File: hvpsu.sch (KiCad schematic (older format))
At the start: 18 parts, among them P1 CONN_01X02, P2 CONN_01X02, SW1 Switch_DPST

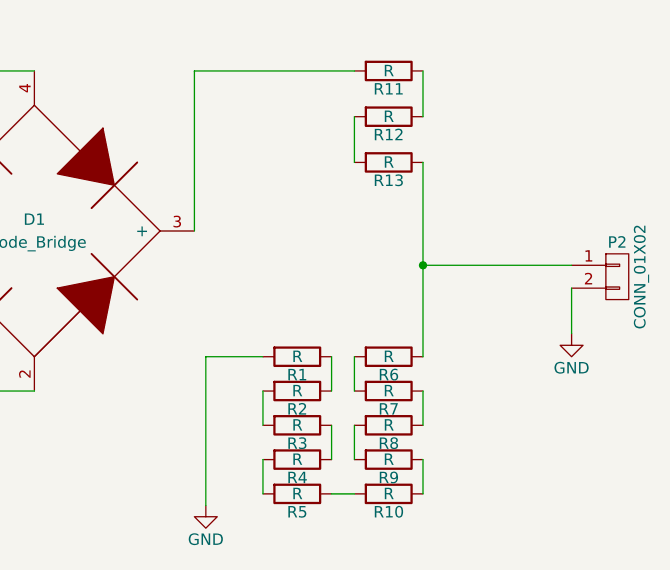
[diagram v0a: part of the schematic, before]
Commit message: fitlering cap and annotations
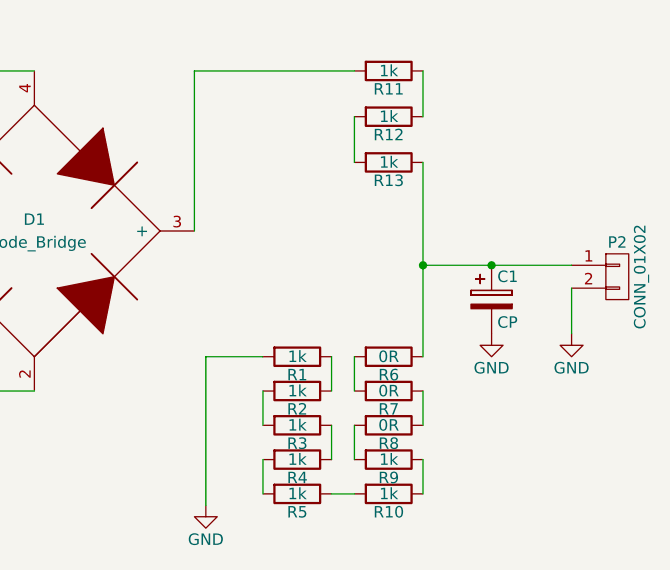
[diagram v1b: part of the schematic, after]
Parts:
- added C1: CP, symbol CP
- R1, R10, R11, R12, R13, R2, R3, R4, R5, R9: value R -> 1k
- R6, R7, R8: value R -> 0R
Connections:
- net GND: now also C1.2
- net at P2.1 (P1), R13.1, R6.1: now also C1.1
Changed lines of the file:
@@
 P 5650 1300
 F 0 "R11" V 5730 1300 50  0000 C CNN
-F 1 "R" V 5650 1300 50  0000 C CNN
+F 1 "1k" V 5650 1300 50  0000 C CNN
 F 2 "" V 5580 1300 30  0000 C CNN
 F 3 "" H 5650 1300 30  0000 C CNN
@@
 P 5650 1500
 F 0 "R12" V 5730 1500 50  0000 C CNN
-F 1 "R" V 5650 1500 50  0000 C CNN
+F 1 "1k" V 5650 1500 50  0000 C CNN
 F 2 "" V 5580 1500 30  0000 C CNN
 F 3 "" H 5650 1500 30  0000 C CNN
@@
 P 5650 1700
 F 0 "R13" V 5730 1700 50  0000 C CNN
-F 1 "R" V 5650 1700 50  0000 C CNN
+F 1 "1k" V 5650 1700 50  0000 C CNN
 F 2 "" V 5580 1700 30  0000 C CNN
 F 3 "" H 5650 1700 30  0000 C CNN
@@
 P 5250 3150
 F 0 "R5" V 5330 3150 50  0000 C CNN
-F 1 "R" V 5250 3150 50  0000 C CNN
+F 1 "1k" V 5250 3150 50  0000 C CNN
 F 2 "" V 5180 3150 30  0000 C CNN
 F 3 "" H 5250 3150 30  0000 C CNN
@@
 P 5250 3000
 F 0 "R4" V 5330 3000 50  0000 C CNN
-F 1 "R" V 5250 3000 50  0000 C CNN
+F 1 "1k" V 5250 3000 50  0000 C CNN
 F 2 "" V 5180 3000 30  0000 C CNN
 F 3 "" H 5250 3000 30  0000 C CNN
@@
 P 5250 2850
 F 0 "R3" V 5330 2850 50  0000 C CNN
-F 1 "R" V 5250 2850 50  0000 C CNN
+F 1 "1k" V 5250 2850 50  0000 C CNN
 F 2 "" V 5180 2850 30  0000 C CNN
 F 3 "" H 5250 2850 30  0000 C CNN
@@
 P 5250 2700
 F 0 "R2" V 5330 2700 50  0000 C CNN
-F 1 "R" V 5250 2700 50  0000 C CNN
+F 1 "1k" V 5250 2700 50  0000 C CNN
 F 2 "" V 5180 2700 30  0000 C CNN
 F 3 "" H 5250 2700 30  0000 C CNN
@@
 P 5250 2550
 F 0 "R1" V 5330 2550 50  0000 C CNN
-F 1 "R" V 5250 2550 50  0000 C CNN
+F 1 "1k" V 5250 2550 50  0000 C CNN
 F 2 "" V 5180 2550 30  0000 C CNN
 F 3 "" H 5250 2550 30  0000 C CNN
 	1    5250 2550
-	0    1    1    0
-$EndComp
-$Comp
-L R R6
-U 1 1 557434CE
-P 5650 2550
-F 0 "R6" V 5730 2550 50  0000 C CNN
-F 1 "R" V 5650 2550 50  0000 C CNN
-F 2 "" V 5580 2550 30  0000 C CNN
-F 3 "" H 5650 2550 30  0000 C CNN
-	1    5650 2550
-	0    1    1    0
-$EndComp
-$Comp
-L R R7
-U 1 1 5574350A
-P 5650 2700
-F 0 "R7" V 5730 2700 50  0000 C CNN
-F 1 "R" V 5650 2700 50  0000 C CNN
-F 2 "" V 5580 2700 30  0000 C CNN
-F 3 "" H 5650 2700 30  0000 C CNN
-	1    5650 2700
-	0    1    1    0
-$EndComp
-$Comp
-L R R8
-U 1 1 5574353C
-P 5650 2850
-F 0 "R8" V 5730 2850 50  0000 C CNN
-F 1 "R" V 5650 2850 50  0000 C CNN
-F 2 "" V 5580 2850 30  0000 C CNN
-F 3 "" H 5650 2850 30  0000 C CNN
-	1    5650 2850
 	0    1    1    0
 $EndComp
@@
 P 5650 3000
 F 0 "R9" V 5730 3000 50  0000 C CNN
-F 1 "R" V 5650 3000 50  0000 C CNN
+F 1 "1k" V 5650 3000 50  0000 C CNN
 F 2 "" V 5580 3000 30  0000 C CNN
 F 3 "" H 5650 3000 30  0000 C CNN
@@
 P 5650 3150
 F 0 "R10" V 5730 3150 50  0000 C CNN
-F 1 "R" V 5650 3150 50  0000 C CNN
+F 1 "1k" V 5650 3150 50  0000 C CNN
 F 2 "" V 5580 3150 30  0000 C CNN
 F 3 "" H 5650 3150 30  0000 C CNN
@@
 	0    1    1    0
 $EndComp
-Wire Wire Line
-	900  1300 1800 1300
-Wire Wire Line
-	900  1700 1800 1700
-Wire Wire Line
-	2400 1300 2950 1300
-Wire Wire Line
-	3450 1300 4100 1300
-Wire Wire Line
-	3400 2000 3400 3200
-Wire Wire Line
-	4100 2700 3150 2700
-Wire Wire Line
-	3150 2700 3150 1700
-Wire Wire Line
-	3150 1700 2400 1700
-Wire Wire Line
-	4800 2000 4800 1300
-Wire Wire Line
-	4800 1300 5500 1300
-Wire Wire Line
-	5800 1300 5800 1500
-Wire Wire Line
-	5500 1500 5500 1700
-Wire Wire Line
-	5800 1700 5800 2550
-Wire Wire Line
-	5100 2550 4850 2550
-Wire Wire Line
-	4850 2550 4850 3200
-Wire Wire Line
-	5400 2550 5400 2700
-Wire Wire Line
-	5100 2700 5100 2850
-Wire Wire Line
-	5400 2850 5400 3000
-Wire Wire Line
-	5100 3000 5100 3150
-Wire Wire Line
-	5400 3150 5500 3150
-Wire Wire Line
-	5800 3150 5800 3000
-Wire Wire Line
-	5500 3000 5500 2850
-Wire Wire Line
-	5800 2850 5800 2700
-Wire Wire Line
-	5500 2700 5500 2550
-$Comp
-L GND #PWR1
+$Comp
+L GND #PWR01
 U 1 1 557438FF
 P 3400 3200
-F 0 "#PWR1" H 3400 2950 50  0001 C CNN
+F 0 "#PWR01" H 3400 2950 50  0001 C CNN
 F 1 "GND" H 3400 3050 50  0000 C CNN
 F 2 "" H 3400 3200 60  0000 C CNN
@@
 $EndComp
 $Comp
-L GND #PWR2
+L GND #PWR02
 U 1 1 55743931
 P 4850 3200
-F 0 "#PWR2" H 4850 2950 50  0001 C CNN
+F 0 "#PWR02" H 4850 2950 50  0001 C CNN
 F 1 "GND" H 4850 3050 50  0000 C CNN
 F 2 "" H 4850 3200 60  0000 C CNN
@@
 	1    0    0    -1
 $EndComp
-Wire Wire Line
-	5800 2150 6450 2150
-Connection ~ 5800 2150
-$Comp
-L GND #PWR3
+$Comp
+L GND #PWR03
 U 1 1 55743988
 P 6450 2450
-F 0 "#PWR3" H 6450 2200 50  0001 C CNN
+F 0 "#PWR03" H 6450 2200 50  0001 C CNN
 F 1 "GND" H 6450 2300 50  0000 C CNN
 F 2 "" H 6450 2450 60  0000 C CNN
@@
 	1    0    0    -1
 $EndComp
-Wire Wire Line
-	6450 2250 6450 2450
 $Comp
 L CONN_01X02 P1
@@
 	-1   0    0    1
 $EndComp
-Wire Wire Line
-	900  1300 900  1450
-Wire Wire Line
-	900  1700 900  1550
 $Comp
 L CONN_01X02 P2
@@
 $EndComp
 $Comp
-L PWR_FLAG #FLG1
+L PWR_FLAG #FLG04
 U 1 1 55743C8C
 P 1800 1300
-F 0 "#FLG1" H 1800 1395 50  0001 C CNN
+F 0 "#FLG04" H 1800 1395 50  0001 C CNN
 F 1 "PWR_FLAG" H 1800 1480 50  0000 C CNN
 F 2 "" H 1800 1300 60  0000 C CNN
@@
 $EndComp
 $Comp
-L PWR_FLAG #FLG2
+L PWR_FLAG #FLG05
 U 1 1 55743CFC
 P 2400 1300
-F 0 "#FLG2" H 2400 1395 50  0001 C CNN
+F 0 "#FLG05" H 2400 1395 50  0001 C CNN
 F 1 "PWR_FLAG" H 2400 1480 50  0000 C CNN
 F 2 "" H 2400 1300 60  0000 C CNN
@@
 $EndComp
 $Comp
-L PWR_FLAG #FLG5
+L PWR_FLAG #FLG06
 U 1 1 55743E75
 P 3450 1300
-F 0 "#FLG5" H 3450 1395 50  0001 C CNN
+F 0 "#FLG06" H 3450 1395 50  0001 C CNN
 F 1 "PWR_FLAG" H 3450 1480 50  0000 C CNN
 F 2 "" H 3450 1300 60  0000 C CNN
@@
 $EndComp
 $Comp
-L PWR_FLAG #FLG4
+L PWR_FLAG #FLG07
 U 1 1 557443CE
 P 3400 2000
-F 0 "#FLG4" H 3400 2095 50  0001 C CNN
+F 0 "#FLG07" H 3400 2095 50  0001 C CNN
 F 1 "PWR_FLAG" H 3400 2180 50  0000 C CNN
 F 2 "" H 3400 2000 60  0000 C CNN
@@
 $EndComp
 $Comp
-L PWR_FLAG #FLG3
+L PWR_FLAG #FLG08
 U 1 1 55744472
 P 3150 1700
-F 0 "#FLG3" H 3150 1795 50  0001 C CNN
+F 0 "#FLG08" H 3150 1795 50  0001 C CNN
 F 1 "PWR_FLAG" H 3150 1880 50  0000 C CNN
 F 2 "" H 3150 1700 60  0000 C CNN
@@
 	1    0    0    -1
 $EndComp
+$Comp
+L CP C1
+U 1 1 5574485B
+P 6100 2300
+F 0 "C1" H 6125 2400 50  0000 L CNN
+F 1 "CP" H 6125 2200 50  0000 L CNN
+F 2 "" H 6138 2150 30  0000 C CNN
+F 3 "" H 6100 2300 60  0000 C CNN
+	1    6100 2300
+	1    0    0    -1
+$EndComp
+$Comp
+L GND #PWR09
+U 1 1 557448C8
+P 6100 2450
+F 0 "#PWR09" H 6100 2200 50  0001 C CNN
+F 1 "GND" H 6100 2300 50  0000 C CNN
+F 2 "" H 6100 2450 60  0000 C CNN
+F 3 "" H 6100 2450 60  0000 C CNN
+	1    6100 2450
+	1    0    0    -1
+$EndComp
+Wire Wire Line
+	900  1300 1800 1300
+Wire Wire Line
+	900  1700 1800 1700
+Wire Wire Line
+	2400 1300 2950 1300
+Wire Wire Line
+	3450 1300 4100 1300
+Wire Wire Line
+	3400 2000 3400 3200
+Wire Wire Line
+	4100 2700 3150 2700
+Wire Wire Line
+	3150 2700 3150 1700
+Wire Wire Line
+	3150 1700 2400 1700
+Wire Wire Line
+	4800 2000 4800 1300
+Wire Wire Line
+	4800 1300 5500 1300
+Wire Wire Line
+	5800 1300 5800 1500
+Wire Wire Line
+	5500 1500 5500 1700
+Wire Wire Line
+	5800 1700 5800 2550
+Wire Wire Line
+	5100 2550 4850 2550
+Wire Wire Line
+	4850 2550 4850 3200
+Wire Wire Line
+	5400 2550 5400 2700
+Wire Wire Line
+	5100 2700 5100 2850
+Wire Wire Line
+	5400 2850 5400 3000
+Wire Wire Line
+	5100 3000 5100 3150
+Wire Wire Line
+	5400 3150 5500 3150
+Wire Wire Line
+	5800 3150 5800 3000
+Wire Wire Line
+	5500 3000 5500 2850
+Wire Wire Line
+	5800 2150 6450 2150
+Connection ~ 5800 2150
+Wire Wire Line
+	6450 2250 6450 2450
+Wire Wire Line
+	900  1300 900  1450
+Wire Wire Line
+	900  1700 900  1550
+Connection ~ 6100 2150
+Wire Wire Line
+	5500 2700 5500 2550
+Wire Wire Line
+	5800 2850 5800 2700
+$Comp
+L R R8
+U 1 1 5574353C
+P 5650 2850
+F 0 "R8" V 5730 2850 50  0000 C CNN
+F 1 "0R" V 5650 2850 50  0000 C CNN
+F 2 "" V 5580 2850 30  0000 C CNN
+F 3 "" H 5650 2850 30  0000 C CNN
+	1    5650 2850
+	0    1    1    0
+$EndComp
+$Comp
+L R R7
+U 1 1 5574350A
+P 5650 2700
+F 0 "R7" V 5730 2700 50  0000 C CNN
+F 1 "0R" V 5650 2700 50  0000 C CNN
+F 2 "" V 5580 2700 30  0000 C CNN
+F 3 "" H 5650 2700 30  0000 C CNN
+	1    5650 2700
+	0    1    1    0
+$EndComp
+$Comp
+L R R6
+U 1 1 557434CE
+P 5650 2550
+F 0 "R6" V 5730 2550 50  0000 C CNN
+F 1 "0R" V 5650 2550 50  0000 C CNN
+F 2 "" V 5580 2550 30  0000 C CNN
+F 3 "" H 5650 2550 30  0000 C CNN
+	1    5650 2550
+	0    1    1    0
+$EndComp
 $EndSCHEMATC

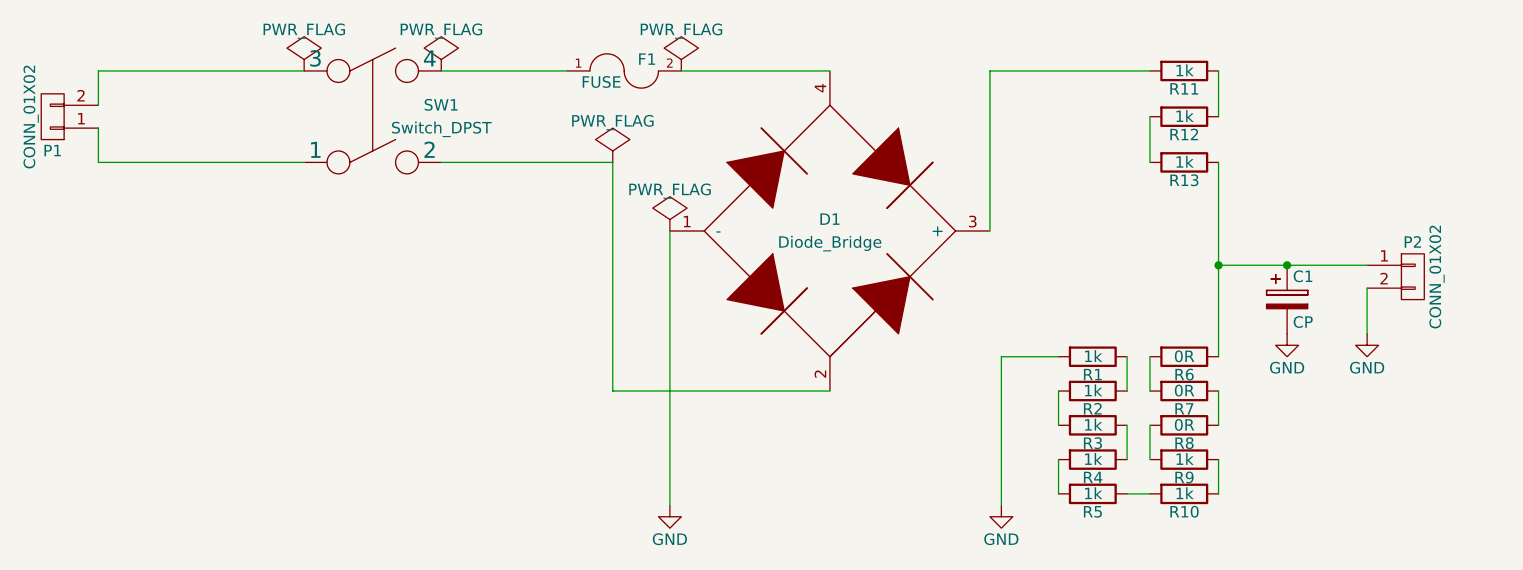
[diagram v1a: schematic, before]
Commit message: most footprints added
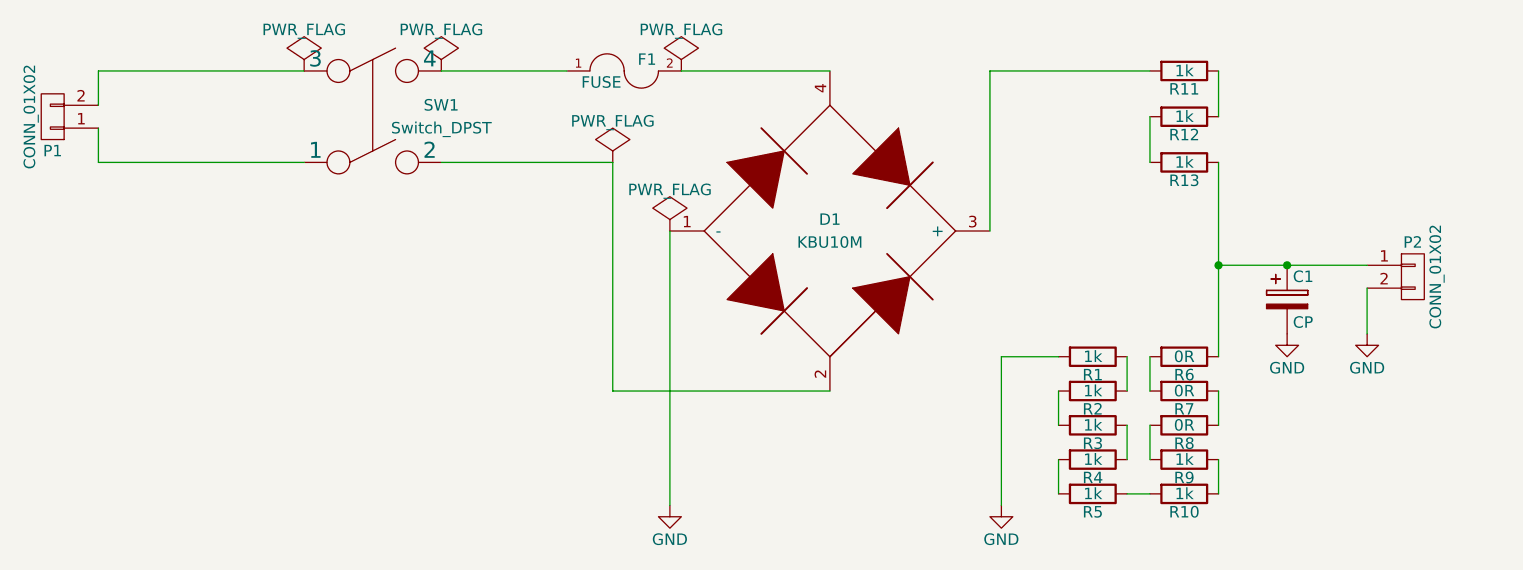
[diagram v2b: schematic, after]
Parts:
- D1: value Diode_Bridge -> KBU10M
- F1: footprint (none) -> Fuse_Holders_and_Fuses:Fuseholder5x20_horiz_open_universal_Type-III
- P1, P2: footprint (none) -> Terminal_Blocks:TerminalBlock_WAGO-236_2Stift_RM5mm_2pol
- R1, R10, R11, R12, R13, R2, R3, R4, R5, R6, R7, R9: footprint (none) -> Resistors_ThroughHole:Resistor_Ceramic_Horizontal_L65mm-W16mm-H15mm-p80mm
- SW1: footprint (none) -> switches:DPST_Rocker_Switch_Chily_3024_Angled
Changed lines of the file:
@@
 LIBS:contrib
 LIBS:valves
+LIBS:hvpsu-cache
 EELAYER 25 0
 EELAYER END
@@
 P 4100 2000
 F 0 "D1" H 4100 2050 50  0000 C CNN
-F 1 "Diode_Bridge" H 4100 1950 50  0000 C CNN
+F 1 "KBU10M" H 4100 1950 50  0000 C CNN
 F 2 "" H 4100 2000 60  0000 C CNN
 F 3 "" H 4100 2000 60  0000 C CNN
@@
 F 0 "F1" H 3300 1350 50  0000 C CNN
 F 1 "FUSE" H 3100 1250 50  0000 C CNN
-F 2 "" H 3200 1300 60  0000 C CNN
+F 2 "Fuse_Holders_and_Fuses:Fuseholder5x20_horiz_open_universal_Type-III" H 3200 1300 60  0001 C CNN
 F 3 "" H 3200 1300 60  0000 C CNN
 	1    3200 1300
@@
 F 0 "SW1" H 2400 1550 50  0000 C CNN
 F 1 "Switch_DPST" H 2400 1450 50  0000 C CNN
-F 2 "" H 2100 1500 60  0000 C CNN
+F 2 "switches:DPST_Rocker_Switch_Chily_3024_Angled" H 2100 1500 60  0001 C CNN
 F 3 "" H 2100 1500 60  0000 C CNN
 	1    2100 1500
@@
 F 0 "R11" V 5730 1300 50  0000 C CNN
 F 1 "1k" V 5650 1300 50  0000 C CNN
-F 2 "" V 5580 1300 30  0000 C CNN
-F 3 "" H 5650 1300 30  0000 C CNN
+F 2 "Resistors_ThroughHole:Resistor_Ceramic_Horizontal_L65mm-W16mm-H15mm-p80mm" V 5580 1300 30  0001 C CNN
+F 3 "" H 5650 1300 30  0001 C CNN
 	1    5650 1300
 	0    1    1    0
@@
 F 0 "R12" V 5730 1500 50  0000 C CNN
 F 1 "1k" V 5650 1500 50  0000 C CNN
-F 2 "" V 5580 1500 30  0000 C CNN
+F 2 "Resistors_ThroughHole:Resistor_Ceramic_Horizontal_L65mm-W16mm-H15mm-p80mm" V 5580 1500 30  0001 C CNN
 F 3 "" H 5650 1500 30  0000 C CNN
 	1    5650 1500
@@
 F 0 "R13" V 5730 1700 50  0000 C CNN
 F 1 "1k" V 5650 1700 50  0000 C CNN
-F 2 "" V 5580 1700 30  0000 C CNN
+F 2 "Resistors_ThroughHole:Resistor_Ceramic_Horizontal_L65mm-W16mm-H15mm-p80mm" V 5580 1700 30  0001 C CNN
 F 3 "" H 5650 1700 30  0000 C CNN
 	1    5650 1700
@@
 F 0 "R5" V 5330 3150 50  0000 C CNN
 F 1 "1k" V 5250 3150 50  0000 C CNN
-F 2 "" V 5180 3150 30  0000 C CNN
+F 2 "Resistors_ThroughHole:Resistor_Ceramic_Horizontal_L65mm-W16mm-H15mm-p80mm" V 5180 3150 30  0001 C CNN
 F 3 "" H 5250 3150 30  0000 C CNN
 	1    5250 3150
@@
 F 0 "R4" V 5330 3000 50  0000 C CNN
 F 1 "1k" V 5250 3000 50  0000 C CNN
-F 2 "" V 5180 3000 30  0000 C CNN
+F 2 "Resistors_ThroughHole:Resistor_Ceramic_Horizontal_L65mm-W16mm-H15mm-p80mm" V 5180 3000 30  0001 C CNN
 F 3 "" H 5250 3000 30  0000 C CNN
 	1    5250 3000
@@
 F 0 "R3" V 5330 2850 50  0000 C CNN
 F 1 "1k" V 5250 2850 50  0000 C CNN
-F 2 "" V 5180 2850 30  0000 C CNN
+F 2 "Resistors_ThroughHole:Resistor_Ceramic_Horizontal_L65mm-W16mm-H15mm-p80mm" V 5180 2850 30  0001 C CNN
 F 3 "" H 5250 2850 30  0000 C CNN
 	1    5250 2850
@@
 F 0 "R2" V 5330 2700 50  0000 C CNN
 F 1 "1k" V 5250 2700 50  0000 C CNN
-F 2 "" V 5180 2700 30  0000 C CNN
+F 2 "Resistors_ThroughHole:Resistor_Ceramic_Horizontal_L65mm-W16mm-H15mm-p80mm" V 5180 2700 30  0001 C CNN
 F 3 "" H 5250 2700 30  0000 C CNN
 	1    5250 2700
@@
 F 0 "R1" V 5330 2550 50  0000 C CNN
 F 1 "1k" V 5250 2550 50  0000 C CNN
-F 2 "" V 5180 2550 30  0000 C CNN
+F 2 "Resistors_ThroughHole:Resistor_Ceramic_Horizontal_L65mm-W16mm-H15mm-p80mm" V 5180 2550 30  0001 C CNN
 F 3 "" H 5250 2550 30  0000 C CNN
 	1    5250 2550
@@
 F 0 "R9" V 5730 3000 50  0000 C CNN
 F 1 "1k" V 5650 3000 50  0000 C CNN
-F 2 "" V 5580 3000 30  0000 C CNN
+F 2 "Resistors_ThroughHole:Resistor_Ceramic_Horizontal_L65mm-W16mm-H15mm-p80mm" V 5580 3000 30  0001 C CNN
 F 3 "" H 5650 3000 30  0000 C CNN
 	1    5650 3000
@@
 F 0 "R10" V 5730 3150 50  0000 C CNN
 F 1 "1k" V 5650 3150 50  0000 C CNN
-F 2 "" V 5580 3150 30  0000 C CNN
+F 2 "Resistors_ThroughHole:Resistor_Ceramic_Horizontal_L65mm-W16mm-H15mm-p80mm" V 5580 3150 30  0001 C CNN
 F 3 "" H 5650 3150 30  0000 C CNN
 	1    5650 3150
@@
 F 0 "P1" H 700 1650 50  0000 C CNN
 F 1 "CONN_01X02" V 800 1500 50  0000 C CNN
-F 2 "" H 700 1500 60  0000 C CNN
+F 2 "Terminal_Blocks:TerminalBlock_WAGO-236_2Stift_RM5mm_2pol" H 700 1500 60  0001 C CNN
 F 3 "" H 700 1500 60  0000 C CNN
 	1    700  1500
@@
 F 0 "P2" H 6650 2350 50  0000 C CNN
 F 1 "CONN_01X02" V 6750 2200 50  0000 C CNN
-F 2 "" H 6650 2200 60  0000 C CNN
+F 2 "Terminal_Blocks:TerminalBlock_WAGO-236_2Stift_RM5mm_2pol" H 6650 2200 60  0001 C CNN
 F 3 "" H 6650 2200 60  0000 C CNN
 	1    6650 2200
@@
 F 0 "R7" V 5730 2700 50  0000 C CNN
 F 1 "0R" V 5650 2700 50  0000 C CNN
-F 2 "" V 5580 2700 30  0000 C CNN
+F 2 "Resistors_ThroughHole:Resistor_Ceramic_Horizontal_L65mm-W16mm-H15mm-p80mm" V 5580 2700 30  0001 C CNN
 F 3 "" H 5650 2700 30  0000 C CNN
 	1    5650 2700
@@
 F 0 "R6" V 5730 2550 50  0000 C CNN
 F 1 "0R" V 5650 2550 50  0000 C CNN
-F 2 "" V 5580 2550 30  0000 C CNN
+F 2 "Resistors_ThroughHole:Resistor_Ceramic_Horizontal_L65mm-W16mm-H15mm-p80mm" V 5580 2550 30  0001 C CNN
 F 3 "" H 5650 2550 30  0000 C CNN
 	1    5650 2550

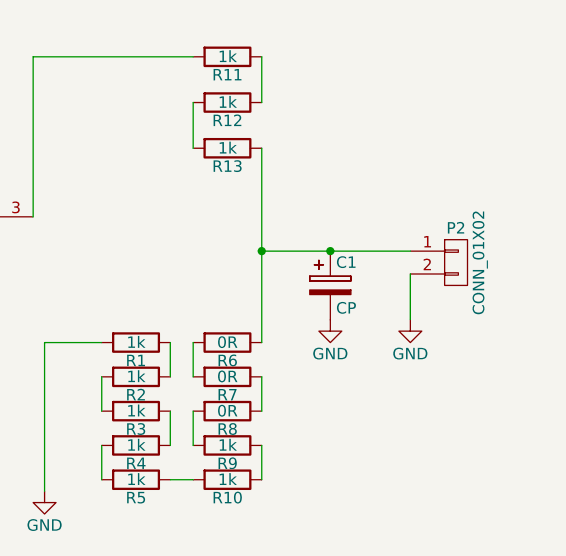
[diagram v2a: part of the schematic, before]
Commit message: all footprints added
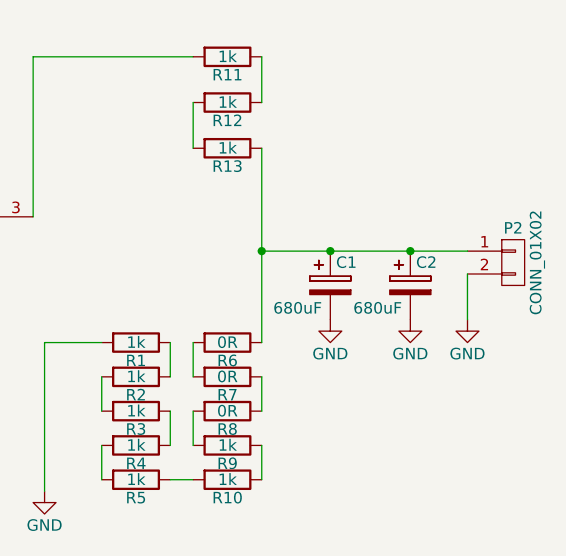
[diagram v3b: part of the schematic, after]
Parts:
- added C2: 680uF, Capacitors_ThroughHole:C_Radial_D35_L51_P10, symbol CP
- C1: value CP -> 680uF; footprint (none) -> Capacitors_ThroughHole:C_Radial_D35_L51_P10
- D1: footprint (none) -> bridges:KBU10M_Bridge_Rectifier_1000V
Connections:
- net GND: now also C2.2
- net at C1.1, P2.1 (P1), R13.1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: now also C2.1
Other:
- moved on the sheet: P2
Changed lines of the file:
@@
 F 0 "D1" H 4100 2050 50  0000 C CNN
 F 1 "KBU10M" H 4100 1950 50  0000 C CNN
-F 2 "" H 4100 2000 60  0000 C CNN
+F 2 "bridges:KBU10M_Bridge_Rectifier_1000V" H 4100 2000 60  0001 C CNN
 F 3 "" H 4100 2000 60  0000 C CNN
 	1    4100 2000
@@
 L GND #PWR03
 U 1 1 55743988
-P 6450 2450
-F 0 "#PWR03" H 6450 2200 50  0001 C CNN
-F 1 "GND" H 6450 2300 50  0000 C CNN
-F 2 "" H 6450 2450 60  0000 C CNN
-F 3 "" H 6450 2450 60  0000 C CNN
-	1    6450 2450
+P 6700 2450
+F 0 "#PWR03" H 6700 2200 50  0001 C CNN
+F 1 "GND" H 6700 2300 50  0000 C CNN
+F 2 "" H 6700 2450 60  0000 C CNN
+F 3 "" H 6700 2450 60  0000 C CNN
+	1    6700 2450
 	1    0    0    -1
 $EndComp
@@
 L CONN_01X02 P2
 U 1 1 55743AAC
-P 6650 2200
-F 0 "P2" H 6650 2350 50  0000 C CNN
-F 1 "CONN_01X02" V 6750 2200 50  0000 C CNN
-F 2 "Terminal_Blocks:TerminalBlock_WAGO-236_2Stift_RM5mm_2pol" H 6650 2200 60  0001 C CNN
-F 3 "" H 6650 2200 60  0000 C CNN
-	1    6650 2200
+P 6900 2200
+F 0 "P2" H 6900 2350 50  0000 C CNN
+F 1 "CONN_01X02" V 7000 2200 50  0000 C CNN
+F 2 "Terminal_Blocks:TerminalBlock_WAGO-236_2Stift_RM5mm_2pol" H 6900 2200 60  0001 C CNN
+F 3 "" H 6900 2200 60  0000 C CNN
+	1    6900 2200
 	1    0    0    -1
 $EndComp
@@
 P 6100 2300
 F 0 "C1" H 6125 2400 50  0000 L CNN
-F 1 "CP" H 6125 2200 50  0000 L CNN
-F 2 "" H 6138 2150 30  0000 C CNN
+F 1 "680uF" H 5850 2200 50  0000 L CNN
+F 2 "Capacitors_ThroughHole:C_Radial_D35_L51_P10" H 6138 2150 30  0001 C CNN
 F 3 "" H 6100 2300 60  0000 C CNN
 	1    6100 2300
@@
 	5500 3000 5500 2850
 Wire Wire Line
-	5800 2150 6450 2150
+	5800 2150 6700 2150
 Connection ~ 5800 2150
 Wire Wire Line
-	6450 2250 6450 2450
+	6700 2250 6700 2450
 Wire Wire Line
 	900  1300 900  1450
@@
 	0    1    1    0
 $EndComp
+$Comp
+L CP C2
+U 1 1 55806817
+P 6450 2300
+F 0 "C2" H 6475 2400 50  0000 L CNN
+F 1 "680uF" H 6200 2200 50  0000 L CNN
+F 2 "Capacitors_ThroughHole:C_Radial_D35_L51_P10" H 6488 2150 30  0001 C CNN
+F 3 "" H 6450 2300 60  0000 C CNN
+	1    6450 2300
+	1    0    0    -1
+$EndComp
+Connection ~ 6450 2150
+$Comp
+L GND #PWR010
+U 1 1 55806893
+P 6450 2450
+F 0 "#PWR010" H 6450 2200 50  0001 C CNN
+F 1 "GND" H 6450 2300 50  0000 C CNN
+F 2 "" H 6450 2450 60  0000 C CNN
+F 3 "" H 6450 2450 60  0000 C CNN
+	1    6450 2450
+	1    0    0    -1
+$EndComp
 $EndSCHEMATC
